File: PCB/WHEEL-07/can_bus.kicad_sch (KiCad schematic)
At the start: 8 parts, among them IC1 TS5A21366DCUR, U2 MCP2561-E-SN, U3 MCP2561-E-SN

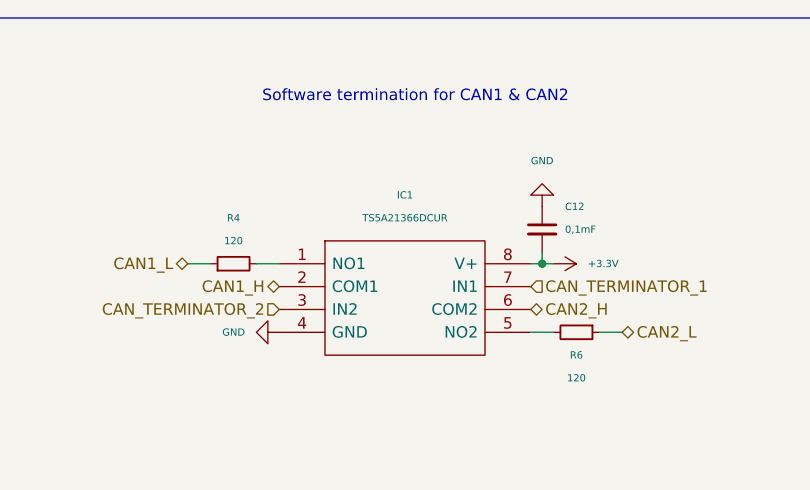
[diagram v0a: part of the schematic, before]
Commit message: Modified layout
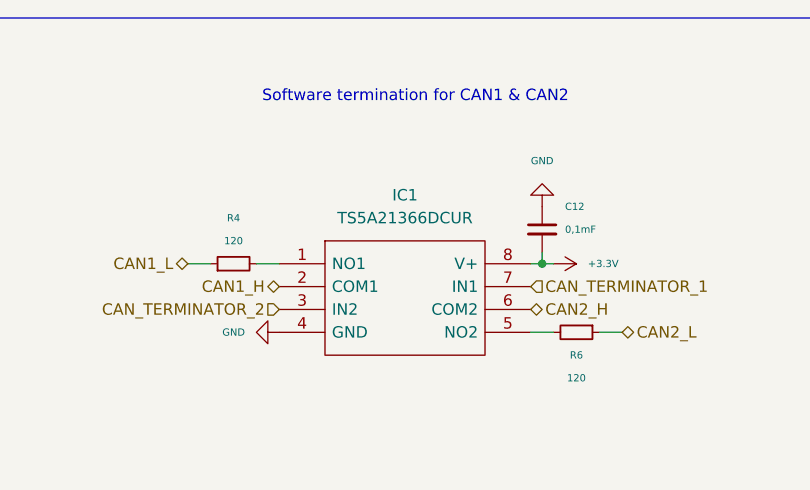
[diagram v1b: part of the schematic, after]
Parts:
- removed IC1: TS5A21366DCUR, PDM_Additional:SOP50P310X90-8N, symbol PDM_additional:TS5A21366DCUR
- added IC1: TS5A21366DCUR, PDM_Additional:SOP50P310X90-8N, symbol WHEEL_07:TS5A21366DCUR
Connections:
- net +3.3V: now also IC1.8 (V+)
- net CAN1_H: now also IC1.2 (COM1)
- net CAN2_H: now also IC1.6 (COM2)
- net CAN_TERMINATOR_1: now also IC1.7 (IN1)
- net CAN_TERMINATOR_2: now also IC1.3 (IN2)
- net GND: now also IC1.4 (GND)
- net at R4.2: now also IC1.1 (NO1)
- net at R6.2: now also IC1.5 (NO2)

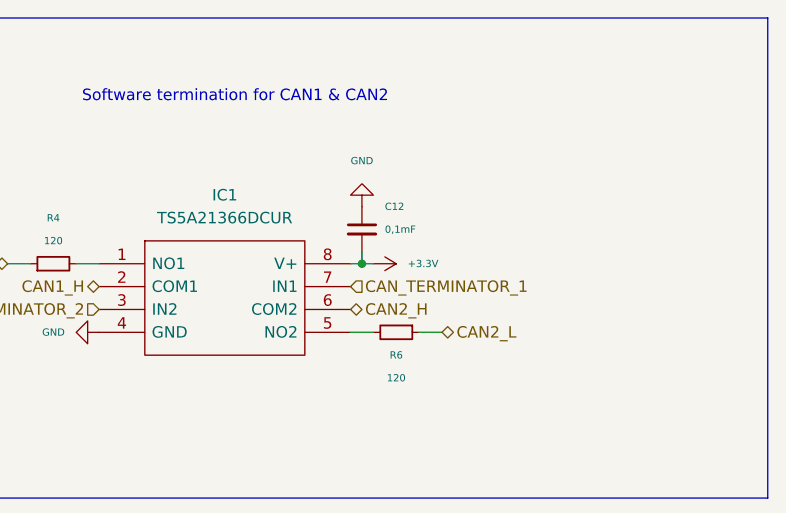
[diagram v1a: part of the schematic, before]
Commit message: Modified schematics & assigned all footprints
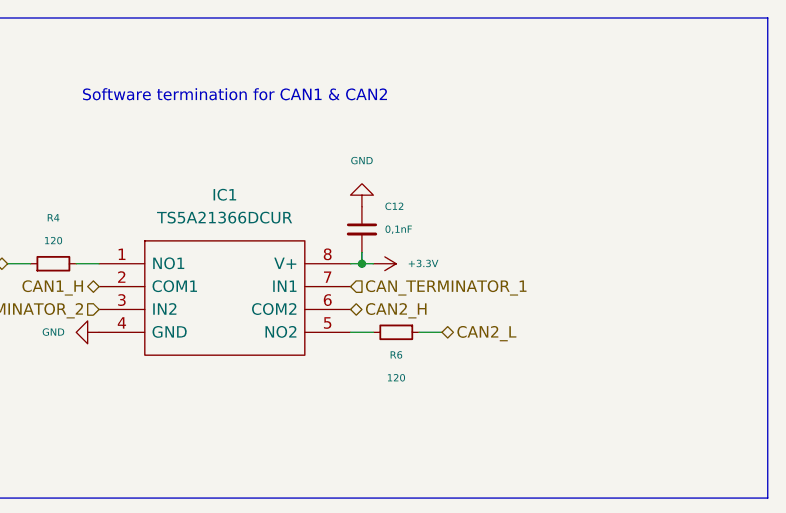
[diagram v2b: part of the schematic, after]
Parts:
- C12: value 0,1mF -> 0,1nF
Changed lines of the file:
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@@
       (effects (font (size 0.8 0.8)) (justify left))
     )
-    (property "Value" "0,1mF" (id 1) (at 155.575 35.56 0)
+    (property "Value" "0,1nF" (id 1) (at 155.575 35.56 0)
       (effects (font (size 0.8 0.8)) (justify left))
     )

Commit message: Changed connectors setup
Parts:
- C12: footprint Capacitor_SMD:C_0805_2012Metric -> Capacitor_SMD:C_0402_1005Metric_Pad0.74x0.62mm_HandSolder
- R4, R6: footprint Resistor_SMD:R_0402_1005Metric -> Resistor_SMD:R_0402_1005Metric_Pad0.72x0.64mm_HandSolder
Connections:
- net CAN1_H: now also R4.1; no longer IC1.2 (COM1)
- net CAN1_L: now also IC1.2 (COM1); no longer R4.1
- net CAN2_H: now also IC1.5 (NO2); no longer IC1.6 (COM2)
- net at R6.2: now also IC1.6 (COM2); no longer IC1.5 (NO2)
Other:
- moved on the sheet: R6
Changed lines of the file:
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@@
     (stroke (width 0) (type default) (color 0 0 0 0))
   )
-  (wire (pts (xy 159.385 46.99) (xy 161.925 46.99))
-    (stroke (width 0) (type default) (color 0 0 0 0))
-  )
-  (wire (pts (xy 151.765 46.99) (xy 154.305 46.99))
+  (wire (pts (xy 159.385 44.45) (xy 161.925 44.45))
+    (stroke (width 0) (type default) (color 0 0 0 0))
+  )
+  (wire (pts (xy 151.765 44.45) (xy 154.305 44.45))
     (stroke (width 0) (type default) (color 0 0 0 0))
   )
@@
     (effects (font (size 1.27 1.27)) (justify left))
   )
-  (hierarchical_label "CAN2_H" (shape bidirectional) (at 151.765 44.45 0)
+  (hierarchical_label "CAN2_H" (shape bidirectional) (at 151.765 46.99 0)
     (effects (font (size 1.27 1.27)) (justify left))
   )
@@
     (effects (font (size 1.27 1.27)) (justify left))
   )
-  (hierarchical_label "CAN1_H" (shape bidirectional) (at 123.825 41.91 180)
+  (hierarchical_label "CAN1_L" (shape bidirectional) (at 123.825 41.91 180)
     (effects (font (size 1.27 1.27)) (justify right))
   )
@@
     (effects (font (size 1.27 1.27)) (justify right))
   )
-  (hierarchical_label "CAN1_L" (shape bidirectional) (at 113.665 39.37 180)
+  (hierarchical_label "CAN1_H" (shape bidirectional) (at 113.665 39.37 180)
     (effects (font (size 1.27 1.27)) (justify right))
   )
-  (hierarchical_label "CAN2_L" (shape bidirectional) (at 161.925 46.99 0)
+  (hierarchical_label "CAN2_L" (shape bidirectional) (at 161.925 44.45 0)
     (effects (font (size 1.27 1.27)) (justify left))
   )
@@
     (pin "2")
   )
-  (symbol (lib_id "Device:R_Small") (at 156.845 46.99 270) (unit 1)
-    (in_bom yes) (on_board yes)
-    (property "Reference" "R6" (id 0) (at 156.845 49.53 90)
+  (symbol (lib_id "Device:R_Small") (at 156.845 44.45 270) (unit 1)
+    (in_bom yes) (on_board yes)
+    (property "Reference" "R6" (id 0) (at 153.035 43.815 90)
       (effects (font (size 0.8 0.8)))
     )
-    (property "Value" "120" (id 1) (at 156.845 52.07 90)
+    (property "Value" "120" (id 1) (at 156.845 44.45 90)
       (effects (font (size 0.8 0.8)))
     )
-    (property "Footprint" "Resistor_SMD:R_0402_1005Metric" (id 2) (at 156.845 46.99 0)
-      (effects (font (size 1.27 1.27)) hide)
-    )
-    (property "Datasheet" "~" (id 3) (at 156.845 46.99 0)
+    (property "Footprint" "Resistor_SMD:R_0402_1005Metric_Pad0.72x0.64mm_HandSolder" (id 2) (at 156.845 44.45 0)
+      (effects (font (size 1.27 1.27)) hide)
+    )
+    (property "Datasheet" "~" (id 3) (at 156.845 44.45 0)
       (effects (font (size 1.27 1.27)) hide)
     )
@@
       (effects (font (size 0.8 0.8)) (justify left))
     )
-    (property "Footprint" "Capacitor_SMD:C_0805_2012Metric" (id 2) (at 153.035 35.56 0)
+    (property "Footprint" "Capacitor_SMD:C_0402_1005Metric_Pad0.74x0.62mm_HandSolder" (id 2) (at 153.035 35.56 0)
       (effects (font (size 1.27 1.27)) hide)
     )
@@
       (effects (font (size 0.8 0.8)))
     )
-    (property "Footprint" "Resistor_SMD:R_0402_1005Metric" (id 2) (at 118.745 39.37 0)
-      (effects (font (size 1.27 1.27)) hide)
-    )
+    (property "Footprint" "Resistor_SMD:R_0402_1005Metric_Pad0.72x0.64mm_HandSolder" (id 2) (at 118.745 39.37 0)
+      (effects (font (size 1.27 1.27)) hide)
+    )

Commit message: Finished layout
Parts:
- removed C10, C11: 0.1u, symbol Device:C_Small
- removed C12: 0,1nF, Capacitor_SMD:C_0402_1005Metric_Pad0.74x0.62mm_HandSolder, symbol Device:C_Small
- removed IC1: TS5A21366DCUR, PDM_Additional:SOP50P310X90-8N, symbol WHEEL_07:TS5A21366DCUR
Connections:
- net CAN1_L: now also R4.2
- net CAN2_H: now also R6.2
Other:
- moved on the sheet: R4, R6

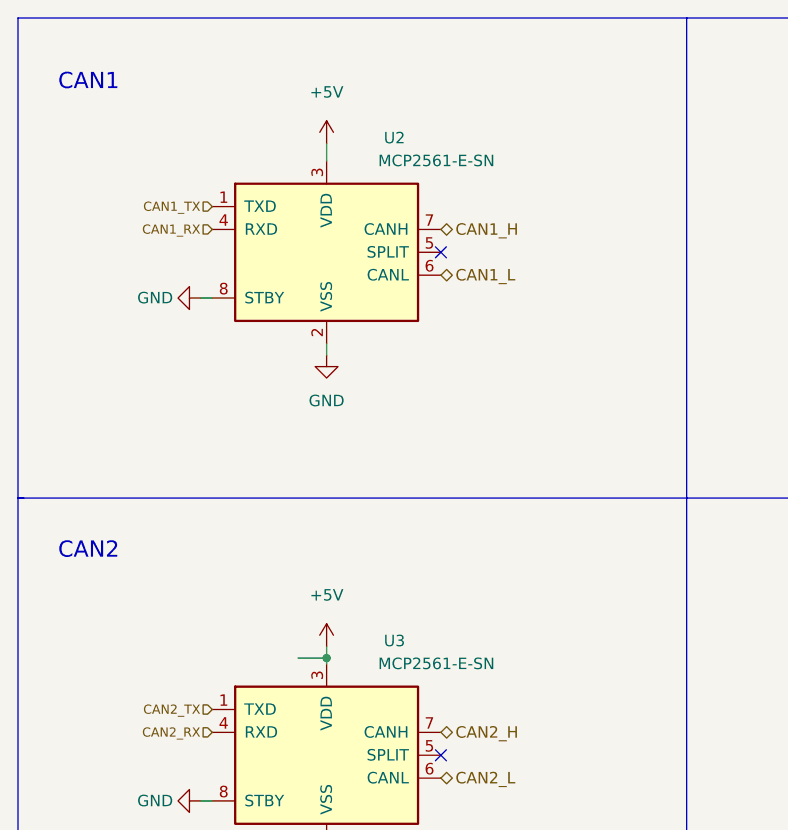
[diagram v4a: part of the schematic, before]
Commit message: Revised board with 2 x LDO40 and cleaned-up schematics
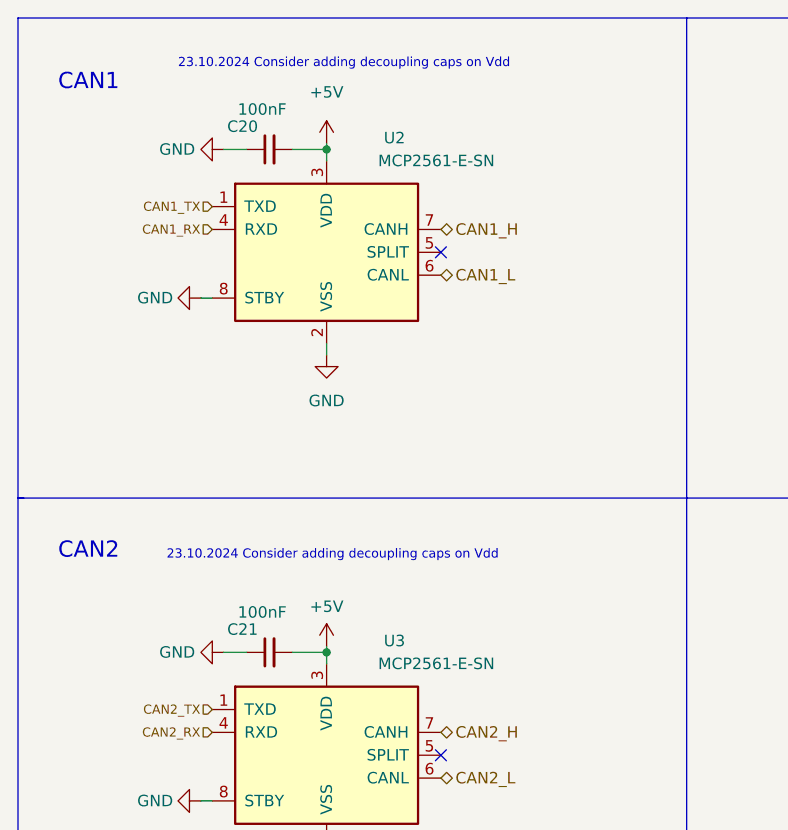
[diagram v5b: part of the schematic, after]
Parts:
- added C20, C21: 100nF, Capacitor_SMD:C_0402_1005Metric_Pad0.74x0.62mm_HandSolder, symbol Device:C_Small
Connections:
- net +5V: now also C20.2, C21.2
- net GND: now also C20.1, C21.1
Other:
- note added: "23.10.2024 Consider adding decoupling caps on Vdd"
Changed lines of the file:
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@@
 (kicad_sch (version 20211123) (generator eeschema)
   (paper "A5")
-  (junction (at 46.355 83.185) (diameter 0) (color 0 0 0 0)
+  (junction (at 46.355 82.55) (diameter 0) (color 0 0 0 0)
+  )
+  (junction (at 46.355 26.67) (diameter 0) (color 0 0 0 0)
   )
   (no_connect (at 59.055 93.98))
   (no_connect (at 59.055 38.1))
-  (wire (pts (xy 43.18 83.185) (xy 46.355 83.185))
-    (stroke (width 0) (type default) (color 0 0 0 0))
-  )
   (polyline (pts (xy 86.36 65.405) (xy 86.36 118.11))
     (stroke (width 0) (type default) (color 0 0 0 0))
@@
     (stroke (width 0) (type default) (color 0 0 0 0))
   )
+  (wire (pts (xy 34.925 26.67) (xy 37.465 26.67))
+    (stroke (width 0) (type default) (color 0 0 0 0))
+  )
   (wire (pts (xy 33.655 43.18) (xy 32.385 43.18))
     (stroke (width 0) (type default) (color 0 0 0 0))
@@
     (stroke (width 0) (type default) (color 0 0 0 0))
   )
+  (wire (pts (xy 46.355 26.67) (xy 46.355 27.94))
+    (stroke (width 0) (type default) (color 0 0 0 0))
+  )
+  (wire (pts (xy 46.355 81.915) (xy 46.355 82.55))
+    (stroke (width 0) (type default) (color 0 0 0 0))
+  )
   (polyline (pts (xy 86.36 12.065) (xy 12.065 12.065))
     (stroke (width 0) (type default) (color 0 0 0 0))
@@
     (stroke (width 0) (type default) (color 0 0 0 0))
   )
-  (wire (pts (xy 46.355 83.185) (xy 46.355 83.82))
+  (wire (pts (xy 46.355 82.55) (xy 46.355 83.82))
     (stroke (width 0) (type default) (color 0 0 0 0))
   )
@@
     (stroke (width 0) (type default) (color 0 0 0 0))
   )
+  (wire (pts (xy 42.545 26.67) (xy 46.355 26.67))
+    (stroke (width 0) (type default) (color 0 0 0 0))
+  )
   (polyline (pts (xy 86.36 118.11) (xy 12.065 118.11))
     (stroke (width 0) (type default) (color 0 0 0 0))
@@
     (stroke (width 0) (type default) (color 0 0 0 0))
   )
-  (wire (pts (xy 46.355 26.035) (xy 46.355 27.94))
+  (wire (pts (xy 46.355 26.035) (xy 46.355 26.67))
     (stroke (width 0) (type default) (color 0 0 0 0))
   )
@@
     (stroke (width 0) (type default) (color 0 0 0 0))
   )
-  (wire (pts (xy 46.355 81.915) (xy 46.355 83.185))
-    (stroke (width 0) (type default) (color 0 0 0 0))
-  )
   (wire (pts (xy 46.355 104.14) (xy 46.355 105.41))
+    (stroke (width 0) (type default) (color 0 0 0 0))
+  )
+  (wire (pts (xy 34.925 82.55) (xy 37.465 82.55))
+    (stroke (width 0) (type default) (color 0 0 0 0))
+  )
+  (wire (pts (xy 42.545 82.55) (xy 46.355 82.55))
     (stroke (width 0) (type default) (color 0 0 0 0))
   )
@@
   (text "CAN2" (at 16.51 72.39 0)
     (effects (font (size 1.8 1.8)) (justify left bottom))
+  )
+  (text "23.10.2024 Consider adding decoupling caps on Vdd" (at 28.575 72.39 0)
+    (effects (font (size 1.016 1.016)) (justify left bottom))
+  )
+  (text "23.10.2024 Consider adding decoupling caps on Vdd" (at 29.845 17.78 0)
+    (effects (font (size 1.016 1.016)) (justify left bottom))
   )
   (hierarchical_label "CAN2_H" (shape bidirectional) (at 59.055 91.44 0)
@@
     (pin "8")
   )
+  (symbol (lib_id "Device:C_Small") (at 40.005 26.67 90) (unit 1)
+    (in_bom yes) (on_board yes)
+    (property "Reference" "C20" (id 0) (at 38.7412 24.13 90)
+      (effects (font (size 1.27 1.27)) (justify left))
+    )
+    (property "Value" "100nF" (id 1) (at 41.91 22.225 90)
+      (effects (font (size 1.27 1.27)) (justify left))
+    )
+    (property "Footprint" "Capacitor_SMD:C_0402_1005Metric_Pad0.74x0.62mm_HandSolder" (id 2) (at 40.005 26.67 0)
+      (effects (font (size 1.27 1.27)) hide)
+    )
+    (property "Datasheet" "~" (id 3) (at 40.005 26.67 0)
+      (effects (font (size 1.27 1.27)) hide)
+    )
+    (pin "1")
+    (pin "2")
+  )
   (symbol (lib_id "Device:R_Small") (at 111.76 36.195 270) (unit 1)
     (in_bom yes) (on_board yes)
@@
     (pin "2")
   )
+  (symbol (lib_id "power:+5V") (at 46.355 81.915 0) (mirror y) (unit 1)
+    (in_bom yes) (on_board yes)
+    (property "Reference" "#PWR0144" (id 0) (at 46.355 85.725 0)
+      (effects (font (size 1.27 1.27)) hide)
+    )
+    (property "Value" "+5V" (id 1) (at 46.355 77.47 0))
+    (property "Footprint" "" (id 2) (at 46.355 81.915 0)
+      (effects (font (size 1.27 1.27)) hide)
+    )
+    (property "Datasheet" "" (id 3) (at 46.355 81.915 0)
+      (effects (font (size 1.27 1.27)) hide)
+    )
+    (pin "1")
+  )
   (symbol (lib_id "power:GND") (at 32.385 99.06 270) (mirror x) (unit 1)
     (in_bom yes) (on_board yes)
@@
     (pin "1")
   )
-  (symbol (lib_id "power:+5V") (at 46.355 81.915 0) (mirror y) (unit 1)
+  (symbol (lib_id "power:GND") (at 34.925 26.67 270) (unit 1)
     (in_bom yes) (on_board yes) (fields_autoplaced)
-    (property "Reference" "#PWR0129" (id 0) (at 46.355 85.725 0)
-      (effects (font (size 1.27 1.27)) hide)
-    )
-    (property "Value" "+5V" (id 1) (at 46.355 76.2 0))
-    (property "Footprint" "" (id 2) (at 46.355 81.915 0)
-      (effects (font (size 1.27 1.27)) hide)
-    )
-    (property "Datasheet" "" (id 3) (at 46.355 81.915 0)
+    (property "Reference" "#PWR0154" (id 0) (at 28.575 26.67 0)
+      (effects (font (size 1.27 1.27)) hide)
+    )
+    (property "Value" "GND" (id 1) (at 31.75 26.6699 90)
+      (effects (font (size 1.27 1.27)) (justify right))
+    )
+    (property "Footprint" "" (id 2) (at 34.925 26.67 0)
+      (effects (font (size 1.27 1.27)) hide)
+    )
+    (property "Datasheet" "" (id 3) (at 34.925 26.67 0)
+      (effects (font (size 1.27 1.27)) hide)
+    )
+    (pin "1")
+  )
+  (symbol (lib_id "power:GND") (at 34.925 82.55 270) (unit 1)
+    (in_bom yes) (on_board yes) (fields_autoplaced)
+    (property "Reference" "#PWR0129" (id 0) (at 28.575 82.55 0)
+      (effects (font (size 1.27 1.27)) hide)
+    )
+    (property "Value" "GND" (id 1) (at 31.75 82.5499 90)
+      (effects (font (size 1.27 1.27)) (justify right))
+    )
+    (property "Footprint" "" (id 2) (at 34.925 82.55 0)
+      (effects (font (size 1.27 1.27)) hide)
+    )
+    (property "Datasheet" "" (id 3) (at 34.925 82.55 0)
       (effects (font (size 1.27 1.27)) hide)
     )
@@
     (pin "8")
   )
+  (symbol (lib_id "Device:C_Small") (at 40.005 82.55 90) (unit 1)
+    (in_bom yes) (on_board yes)
+    (property "Reference" "C21" (id 0) (at 38.7412 80.01 90)
+      (effects (font (size 1.27 1.27)) (justify left))
+    )
+    (property "Value" "100nF" (id 1) (at 41.91 78.105 90)
+      (effects (font (size 1.27 1.27)) (justify left))
+    )
+    (property "Footprint" "Capacitor_SMD:C_0402_1005Metric_Pad0.74x0.62mm_HandSolder" (id 2) (at 40.005 82.55 0)
+      (effects (font (size 1.27 1.27)) hide)
+    )
+    (property "Datasheet" "~" (id 3) (at 40.005 82.55 0)
+      (effects (font (size 1.27 1.27)) hide)
+    )
+    (pin "1")
+    (pin "2")
+  )
   (symbol (lib_id "Device:R_Small") (at 111.76 31.75 90) (unit 1)
